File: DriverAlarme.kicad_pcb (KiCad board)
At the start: 2 copper layers, 18 parts, among them J1 Terminal_Fonte, J2 Terminal_Cerca, J3 Terminal_Alarme, Q1 2N3906, Q2 2N3906

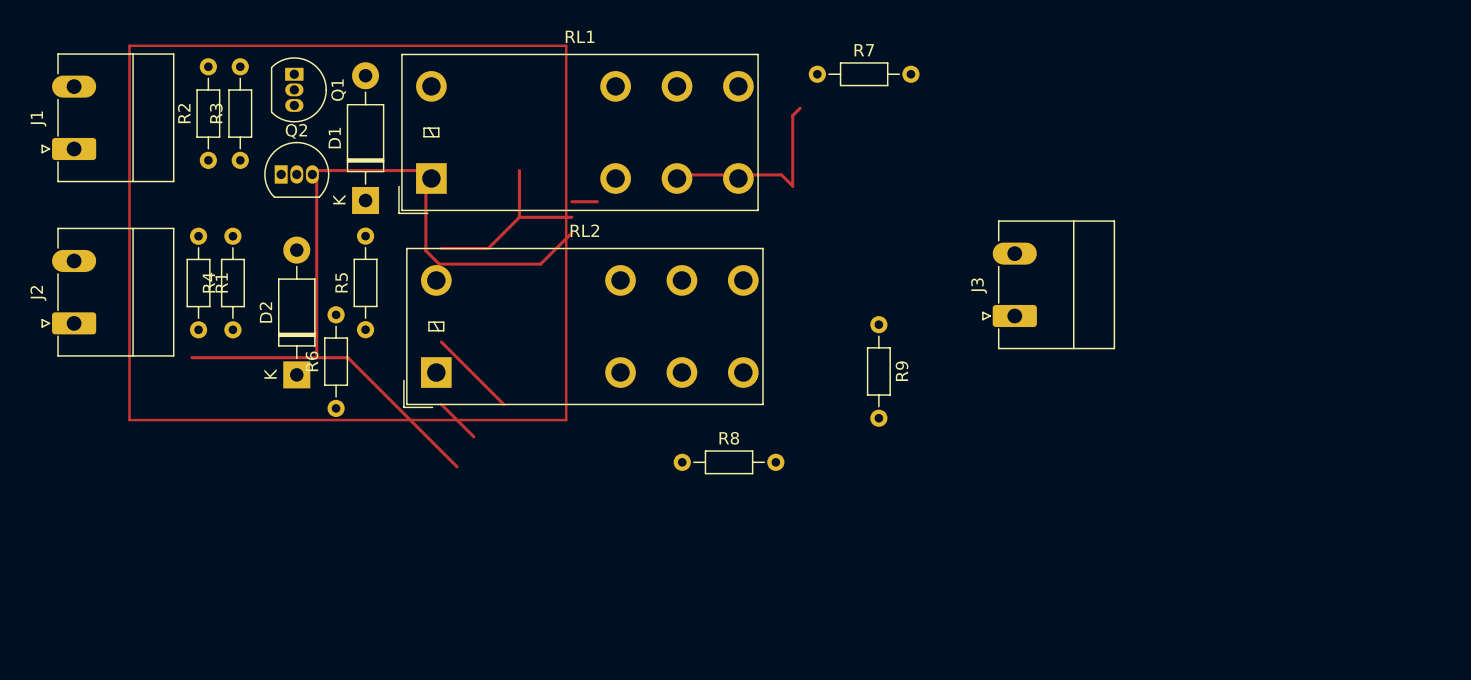
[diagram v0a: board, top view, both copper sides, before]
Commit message: Trimpot for adjust current over transistor
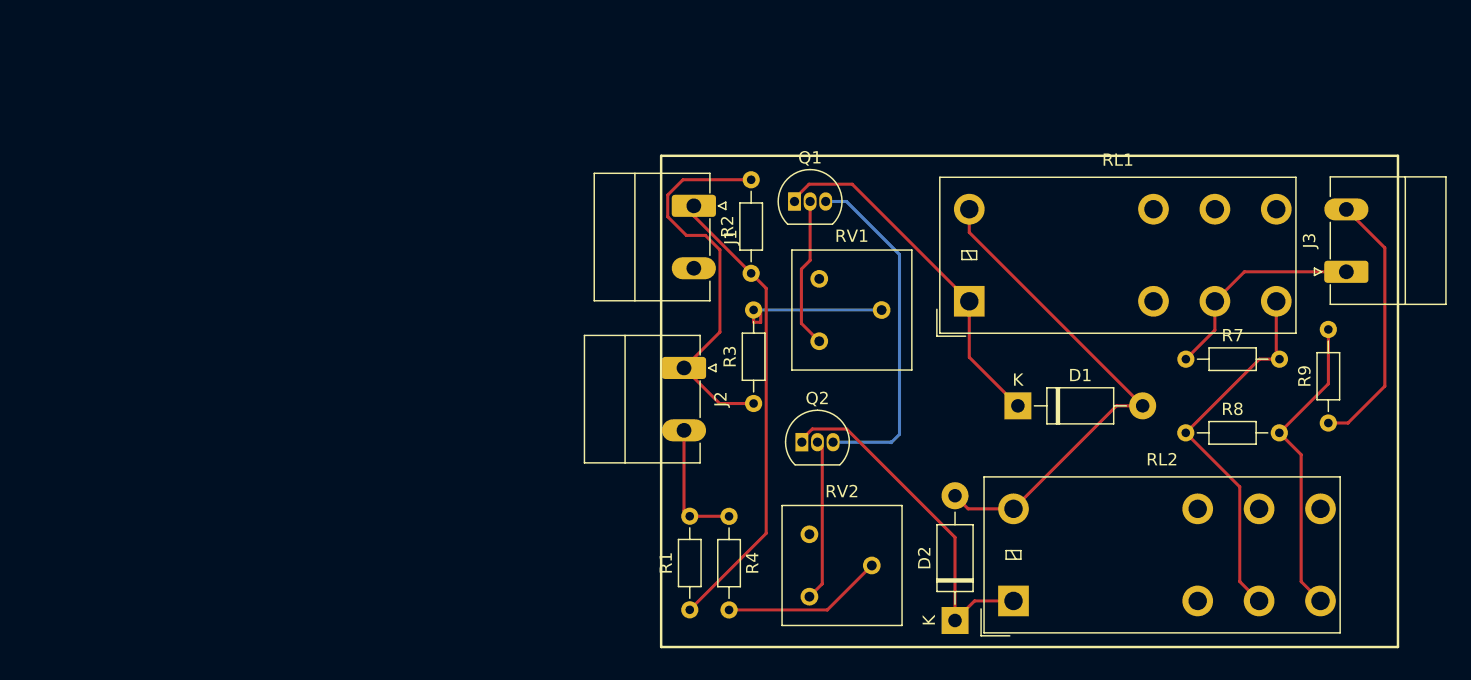
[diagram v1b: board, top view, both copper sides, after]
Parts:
- removed R5, R6: 200 Ohm, Resistor_THT:R_Axial_DIN0204_L3.6mm_D1.6mm_P7.62mm_Horizontal
- added RV1: 0-200K, Potentiometer_THT:Potentiometer_Bourns_3386F_Vertical, F.Cu at (73.9, 54.5)
- added RV2: 0-200K, Potentiometer_THT:Potentiometer_Bourns_3386F_Vertical, F.Cu at (73.1, 75.3)
- R1, R2: value 22 K -> 20 K
- R3, R4: value 2K2 -> 100 K
- moved D2 57.2 mm to (85.0, 77.3)
- moved D1 55.7 mm to (90.1, 59.8), turned to 0 degrees
- moved J1 50.7 mm to (63.7, 43.5), turned to -90 degrees
- moved RL2 50.5 mm to (89.8, 75.7)
- moved R1 50.3 mm to (63.4, 76.4), turned to 90 degrees
- moved J2 49.8 mm to (62.9, 56.7), turned to -90 degrees
- moved Q2 47.7 mm to (72.5, 62.8)
- moved R3 46.3 mm to (68.6, 59.6)
- moved R2 45.1 mm to (68.4, 49.0)
- moved RL1 44.9 mm to (86.2, 51.3)
- moved R4 43.2 mm to (66.6, 68.8), turned to -90 degrees
- moved Q1 42.0 mm to (71.9, 43.2), turned to 0 degrees
- moved R8 41.1 mm to (103.8, 62.0)
- moved R7 37.9 mm to (103.8, 56.0)
- moved R9 37.5 mm to (115.4, 61.2), turned to 90 degrees
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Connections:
- D1 pad 2: Net-(R5-Pad1) -> GND
- D2 pad 2: Net-(D2-Pad2) -> GND
- J2 pad 1: Net-(R3-Pad1) -> Net-(J2-Pad1)
- Q1 pad 3: Net-(J1-Pad1) -> Net-(Q1-Pad3)
- Q2 pad 3: Net-(J1-Pad1) -> Net-(Q1-Pad3)
- R1 pad 2: Net-(Q2-Pad2) -> Net-(J2-Pad2)
- R2 pad 2: Net-(Q1-Pad2) -> Net-(J2-Pad1)
- R3 pad 1: Net-(R3-Pad1) -> Net-(J2-Pad1)
- R3 pad 2: Net-(Q1-Pad2) -> Net-(R3-Pad2)
- R4 pad 1: Net-(Q2-Pad2) -> Net-(J2-Pad2)
- R4 pad 2: Net-(J2-Pad2) -> Net-(R4-Pad2)
- RL1 pad 8: Net-(R5-Pad1) -> GND
- RL2 pad 8: Net-(D2-Pad2) -> GND
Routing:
- net Net-(J2-Pad1): track 0.00 -> 32.1 mm
- net Net-(J1-Pad1): track 69.3 -> 37.9 mm
- net Net-(R7-Pad2): track 0.00 -> 31.1 mm
- net Net-(Q2-Pad1): track 0.00 -> 28.9 mm
- net Net-(Q1-Pad3): track 0.00 -> 28.1 mm
- net Net-(Q1-Pad1): track 2.08 -> 29.0 mm
- net GND: track 15.5 -> 41.1 mm
- net Net-(R8-Pad2): track 0.17 -> 25.1 mm
- net Net-(J3-Pad2): track 0.00 -> 21.7 mm
- net Net-(J3-Pad1): track 0.08 -> 17.4 mm
- net Net-(R5-Pad1): track 15.9 -> 0.00 mm
- net Net-(Q2-Pad2): track 0.00 -> 13.2 mm
- net Net-(R4-Pad2): track 0.00 -> 13.1 mm
- net Net-(R3-Pad2): track 0.00 -> 13.0 mm
- net Net-(Q1-Pad2): track 0.00 -> 12.3 mm
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- removed copper zone on F.Cu, net (none)

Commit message: Changed to wired conector
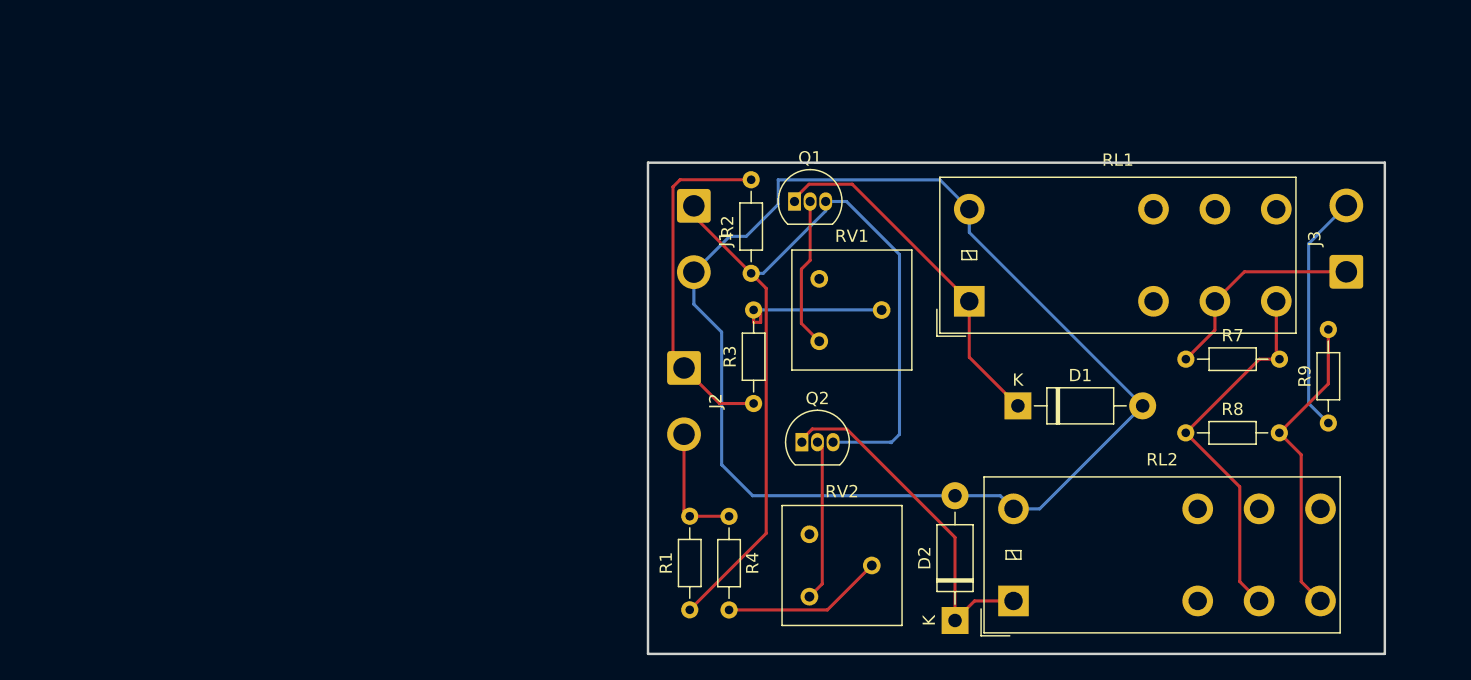
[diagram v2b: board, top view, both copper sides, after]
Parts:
- J1, J2, J3: footprint Connector_Phoenix_MC_HighVoltage:PhoenixContact_MC_1,5_2-G-5.08_1x02_P5.08mm_Horizontal -> Connector_Wire:SolderWire-1sqmm_1x02_P5.4mm_D1.4mm_OD2.7mm
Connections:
- J1 pad 2: Earth -> GND
- Q1 pad 3: Net-(Q1-Pad3) -> Net-(J1-Pad1)
- Q2 pad 3: Net-(Q1-Pad3) -> Net-(J1-Pad1)
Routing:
- net GND: track 41.1 -> 105.7 mm
- net Net-(J1-Pad1): track 37.9 -> 75.0 mm
- net Net-(Q1-Pad3): track 28.1 -> 0.00 mm
- net Net-(J2-Pad1): track 32.1 -> 28.6 mm
- net Net-(J3-Pad2): track 21.7 -> 19.8 mm
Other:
- board outline added: 60 x 40 mm
